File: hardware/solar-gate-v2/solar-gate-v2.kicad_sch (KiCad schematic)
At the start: 27 parts, among them Q1A AO3401, Q1B AO3401, Q2A AO3401, Q2B AO3401, Q3 2N3904, U1 LM393, U2 TL431

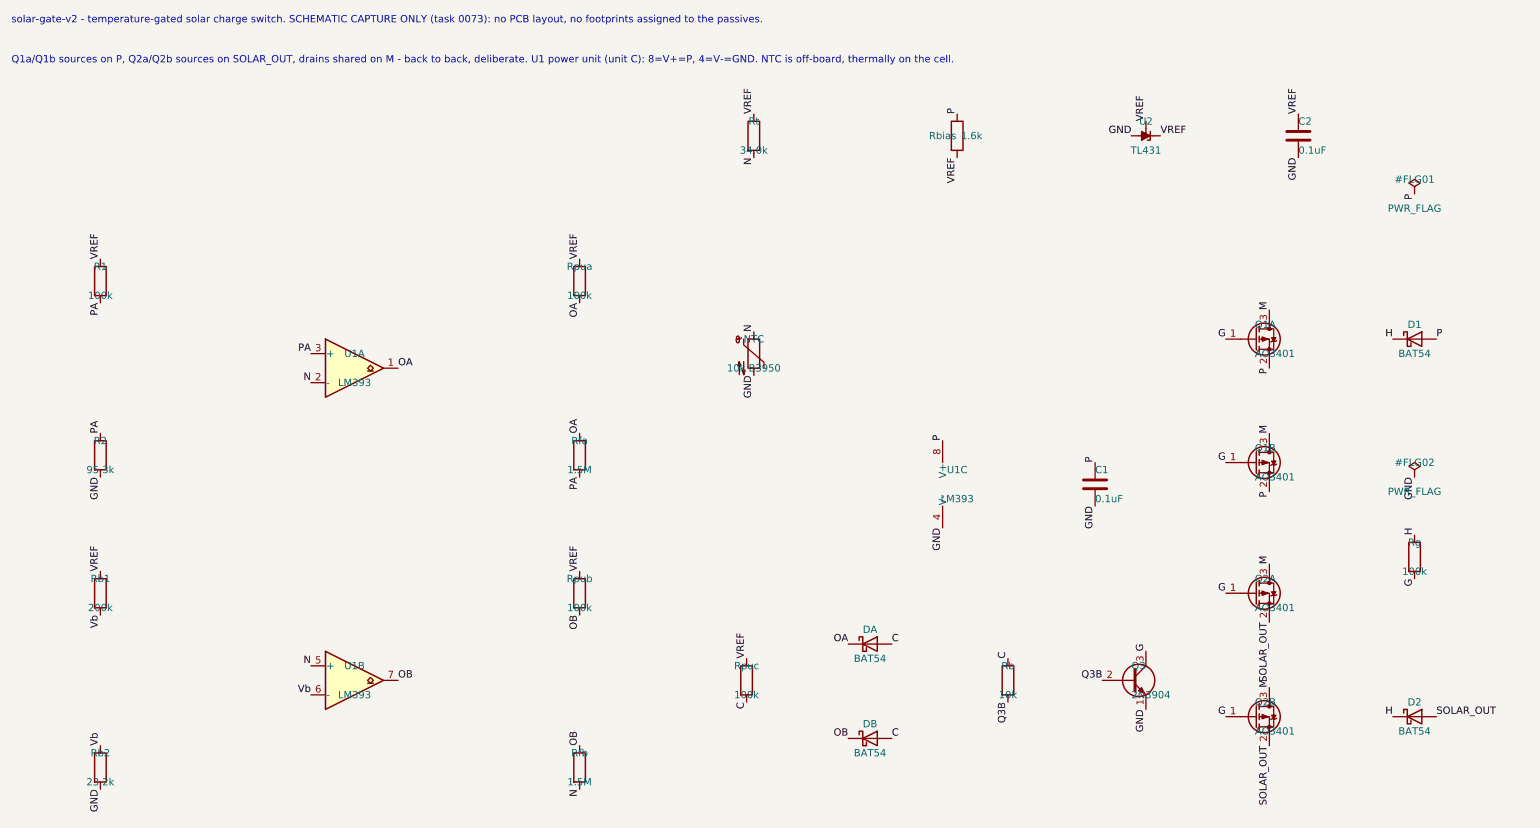
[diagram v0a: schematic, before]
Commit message: 0074: redraw solar-gate-v2 with real wires
Rebuild solar-gate-v2.kicad_sch so every connection is drawn as a wire
instead of a net label: 115 (wire) entries (81 routed segments, broken at
T-points by the tool) and 39 junctions. The 14 net labels remain as
supplements only - the netlist does not depend on them.

Connectivity is unchanged from the 0073 capture: 27 components and 14 nets
with identical membership (checked with generate_netlist against the
preserved 0073 file). ERC: 0 errors, 22 warnings, all lib_symbol_mismatch
(Flatpak KiCad 10 libraries vs the host copies embedded at load).

Layout is rebuilt on the 1.27 mm grid with left-to-right signal flow and
explicit Reference/Value placement: 0 text-over-wire overlaps and 0 real
text-vs-text collisions (measured from the SVG glyph boxes; the 0073 render
had 85 colliding text pairs).

Renders: SVG, PDF and a 600 dpi PNG (7016x4961, A4 landscape) for phone
viewing, plus the refreshed ERC report.

Mailbox: 0074
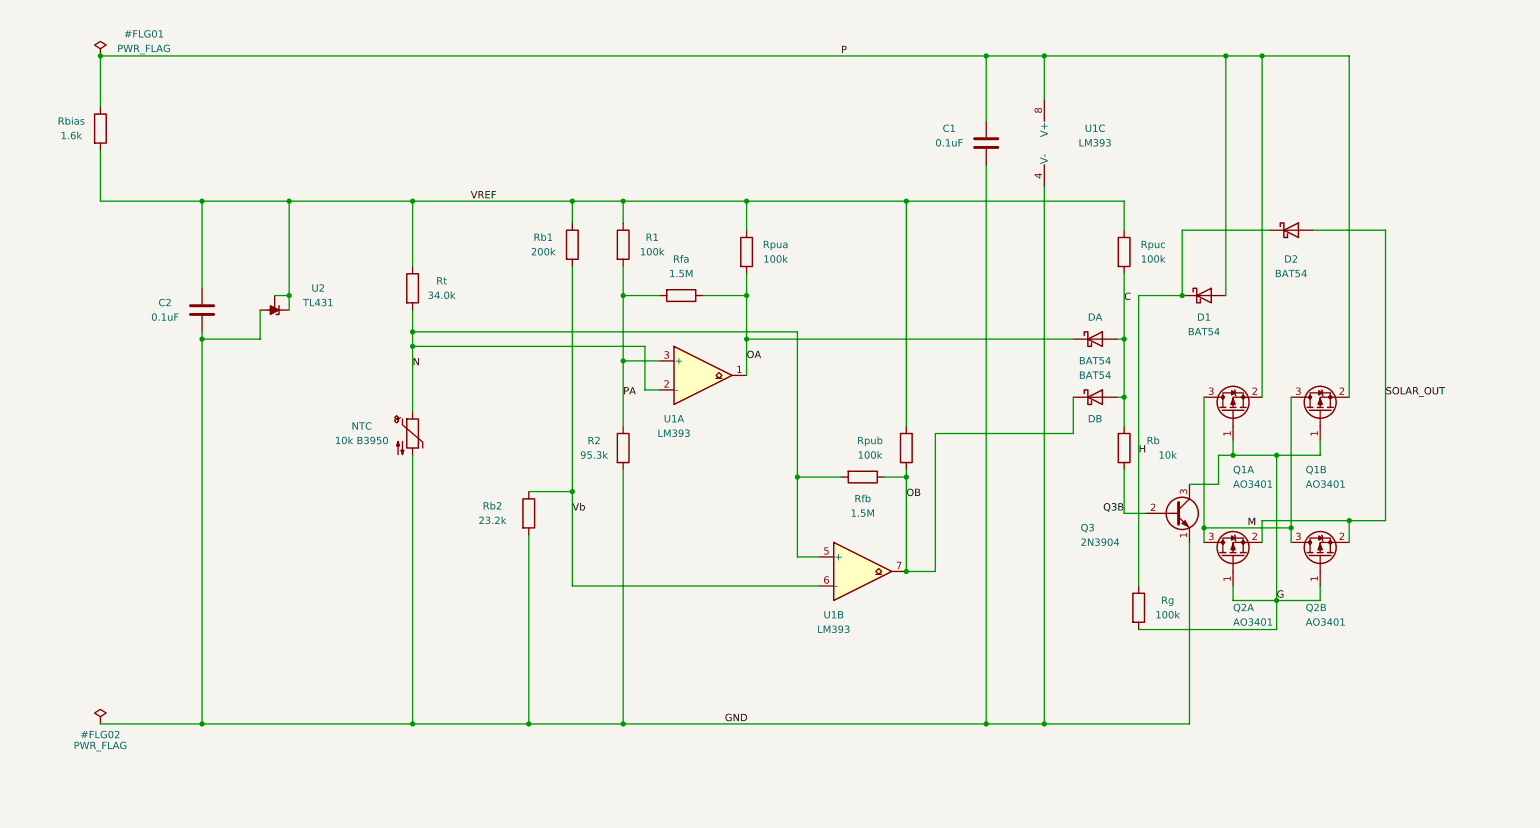
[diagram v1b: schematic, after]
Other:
- note removed: "Q1a/Q1b sources on P, Q2a/Q2b sources on SOLAR_OUT, drains shared on M - back to back, deliberate. U1 power unit (unit C): 8=V+=P, 4=V-=GND. NTC is off-board, thermally on the cell."
- note removed: "solar-gate-v2 - temperature-gated solar charge switch. SCHEMATIC CAPTURE ONLY (task 0073): no PCB layout, no footprints assigned to the passives."

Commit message: 0075: add J1/J2 I/O connectors and device/block labels to solar-gate-v2
- J1 "SOLAR IN" (Conn_01x02, JST GH 1.25mm footprint): pin1 -> P, pin2 -> GND
- J2 "TO HELTEC": pin1 -> SOLAR_OUT, pin2 -> GND
- both wired with real wires to T-taps on the existing P/SOLAR_OUT risers and to
  an extension of the bottom GND rail; staggering chosen so no wire crosses
- NTC lead note + six functional-block annotations (measured 0 collisions)
- ERC 0 errors / 24 warnings (all lib_symbol_mismatch); netlist 14 nets, 29
  components, membership of the original 27 unchanged
- SVG/PNG(7016x4961)/PDF re-exported from the committed revision
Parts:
- added J1: SOLAR IN, Connector_JST:JST_GH_SM02B-GHS-TB_1x02-1MP_P1.25mm_Horizontal, symbol Connector_Generic:Conn_01x02
- added J2: TO HELTEC, Connector_JST:JST_GH_SM02B-GHS-TB_1x02-1MP_P1.25mm_Horizontal, symbol Connector_Generic:Conn_01x02
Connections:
- net GND: now also J1.2 (Pin_2), J2.2 (Pin_2)
- net P: now also J1.1 (Pin_1)
- net SOLAR_OUT: now also J2.1 (Pin_1)
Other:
- note added: "NTC on leads — thermally couple to the battery cell"
- note added: "SOLAR PANEL IN (+/-) — 13 W, 5 V panel"
- note added: "TO HELTEC LoRa 32 V4 SOLAR INPUT — gated charge output"
- note added: "Vref (U2/TL431)"
- note added: "cold comparator"
- note added: "fault-OR (DA/DB)"
- note added: "gate drive (Q3)"
- note added: "hot comparator"
- note added: "pass switch (Q1A/Q1B/Q2A/Q2B back-to-back)"
